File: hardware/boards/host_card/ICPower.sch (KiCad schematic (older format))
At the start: 56 parts, among them J6 SODIMM_260, U1 ECP5UM5G-381caBGA, U3 CYUSB3014, U4 IS43TR16256B-125KBL, U5 128MiB, U6 128MiB, U7 SI5330B, U8 IS43TR16256B-125KBL

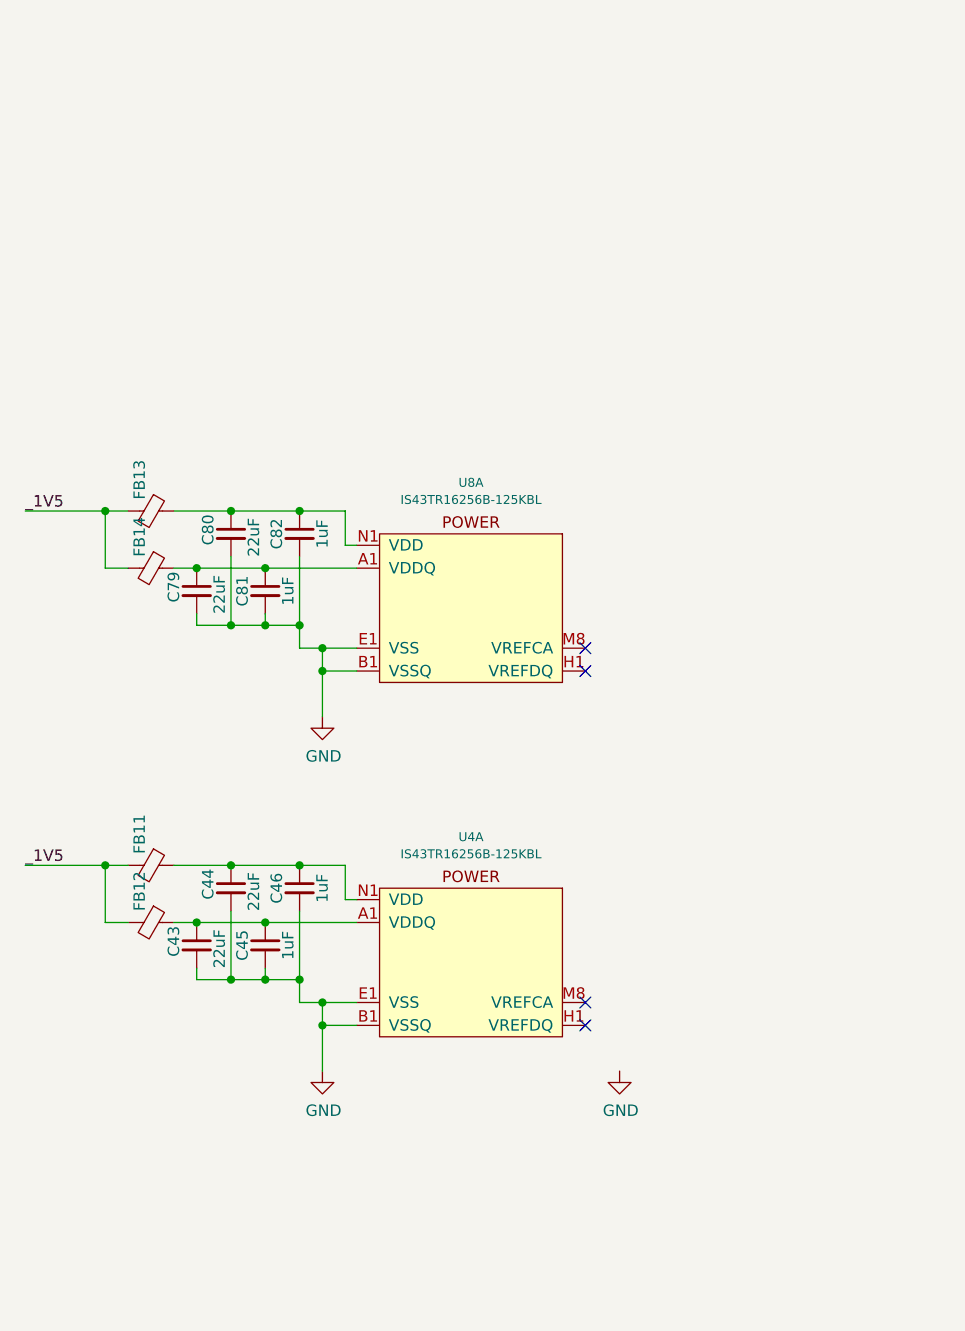
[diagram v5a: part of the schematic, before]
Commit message: Broke out the DDR3 modules and added the 0.75V LDO for the VREFCA and VREFDQ lines for each of the DDR3 modules
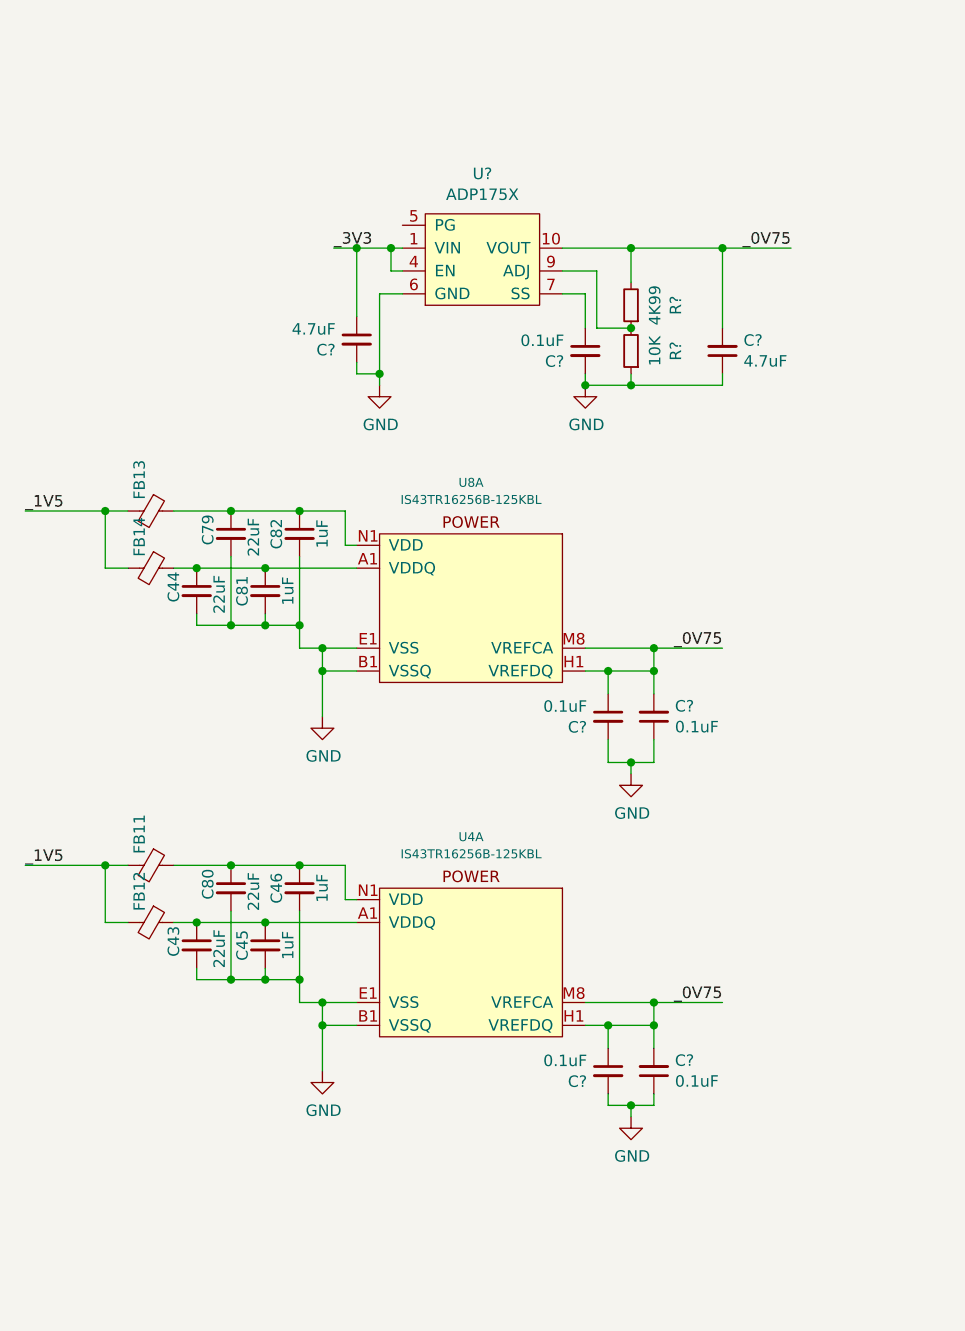
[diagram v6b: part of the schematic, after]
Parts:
- added C? (x5): 0.1uF, Capacitor_SMD:C_0603_1608Metric, symbol Device:C_Small
- added C? (x2): 4.7uF, Capacitor_SMD:C_0603_1608Metric, symbol Device:C_Small
- added R?: 10K, Resistor_SMD:R_0603_1608Metric, symbol Device:R_Small
- added R?: 4K99, Resistor_SMD:R_0603_1608Metric, symbol Device:R_Small
- added U?: ADP175X, Package_DFN_QFN:QFN-16-1EP_4x4mm_P0.65mm_EP2.5x2.5mm, symbol lethalbit:ADP175X
- C43, C44, C79, C80: footprint Capacitor_SMD:C_1206_3216Metric -> Capacitor_SMD:C_0805_2012Metric; MPN C1206C226K9PACTU -> C0805C226K9PAC7800
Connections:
- net 3V3: now also C?.1, U?.1 (VIN), U?.15 (VIN), U?.16 (VIN), U?.2 (VIN), U?.3 (VIN), U?.4 (EN)
- net GND: now also C?.1, C?.1, C?.1, C?.2, C?.2, C?.2, C?.2, R?.1, U?.17 (GND), U?.6 (GND)
- net at C46.1, FB11.1, U4.B2 (VDD)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: now also C80.1; no longer C44.1
- net _0V75: now reaches U4.H1 (VREFDQ)
- net _0V75: now also U4.M8 (VREFCA), U8.H1 (VREFDQ), U8.M8 (VREFCA), C?.1, C?.1, C?.2, C?.2, C?.2, R?.2, U?.10 (VOUT), U?.11 (VOUT), U?.12 (VOUT), U?.13 (VOUT), U?.14 (VOUT)
- net at C81.1, FB14.1, U8.A1 (VDDQ)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: now also C44.1; no longer C79.1
- net at C82.1, FB13.1, U8.B2 (VDD)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: now also C79.1; no longer C80.1
- new net: C?.1, U?.7 (SS)
- new net: R?.1, R?.2, U?.9 (ADJ)
- no-connect marks 10 -> 6

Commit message: Minor cleanup and added some notes
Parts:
- gave numbers to parts that had none: 10
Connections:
- no-connect marks 6 -> 1
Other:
- note added: "TODO: Add the appropriate voltage levels for each bank\n"
- note added: "TODO: Properly add the rest of the bypass caps for the rest of the IO banks."
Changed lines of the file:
@@
 $EndDescr
-$Comp
-L lethalbit:LFE5UM5G-85F-8BG381I U?
-U 1 1 5F21FED7
-P 8500 1700
-AR Path="/5F21FED7" Ref="U?"  Part="1"
-AR Path="/5EF66251/5F21FED7" Ref="U?"  Part="1"
-AR Path="/5EF66188/5F21FED7" Ref="U1"  Part="1"
-F 0 "U1" H 8475 2048 50  0000 C CNN
-F 1 "ECP5UM5G-381caBGA" H 8475 1957 50  0000 C CNN
-F 2 "lethalbit:318caBGA" H 7150 1850 50  0001 C CNN
-F 3 "" H 7150 1850 50  0001 C CNN
-F 4 "Lattice" H 8500 1700 50  0001 C CNN "MFR"
-F 5 "LFE5UM5G-85F-8BG381I" H 8500 1700 50  0001 C CNN "MPN"
-F 6 "220-2112-ND" H 8500 1700 50  0001 C CNN "DIGIKEY_PN"
-	1    8500 1700
-	1    0    0    -1
-$EndComp
 $Comp
 L lethalbit:CYUSB3014 U3
@@
 Wire Wire Line
 	9100 1650 9600 1650
-NoConn ~ 7850 2200
-NoConn ~ 7850 1800
-NoConn ~ 9100 2000
-NoConn ~ 9100 2150
 $Comp
 L Device:C_Small C40
@@
 Text Label 700  9550 0    39   ~ 0
 _3V3
-NoConn ~ 9100 1800
 Wire Wire Line
 	5200 4800 5150 4800
@@
 Wire Wire Line
 	9100 2750 9600 2750
-NoConn ~ 9100 2600
 $Comp
 L lethalbit:SODIMM_260 J6
@@
 	9200 6300 9500 6300
 $Comp
-L lethalbit:ADP175X U?
+L lethalbit:ADP175X U9
 U 1 1 5F9DE092
 P 10300 5150
-F 0 "U?" H 10300 5475 50  0000 C CNN
+F 0 "U9" H 10300 5475 50  0000 C CNN
 F 1 "ADP175X" H 10300 5384 50  0000 C CNN
 F 2 "Package_DFN_QFN:QFN-16-1EP_4x4mm_P0.65mm_EP2.5x2.5mm" H 10300 4750 50  0001 C CNN
@@
 P 10750 5600
 AR Path="/5EDF9F51/5FA82CDE" Ref="C?"  Part="1"
-AR Path="/5EF66188/5FA82CDE" Ref="C?"  Part="1"
-F 0 "C?" H 10658 5554 50  0000 R CNN
+AR Path="/5EF66188/5FA82CDE" Ref="C85"  Part="1"
+F 0 "C85" H 10658 5554 50  0000 R CNN
 F 1 "0.1uF" H 10658 5645 50  0000 R CNN
 F 2 "Capacitor_SMD:C_0603_1608Metric" H 10750 5600 50  0001 C CNN
@@
 	10750 5350 10650 5350
 $Comp
-L power:GND #PWR?
+L power:GND #PWR0149
 U 1 1 5FAB1A8D
 P 10750 5750
-F 0 "#PWR?" H 10750 5500 50  0001 C CNN
+F 0 "#PWR0149" H 10750 5500 50  0001 C CNN
 F 1 "GND" H 10755 5577 50  0000 C CNN
 F 2 "" H 10750 5750 50  0001 C CNN
@@
 P 11350 5600
 AR Path="/5EDF9F51/5FB87077" Ref="C?"  Part="1"
-AR Path="/5EF66188/5FB87077" Ref="C?"  Part="1"
-F 0 "C?" H 11258 5554 50  0000 R CNN
+AR Path="/5EF66188/5FB87077" Ref="C90"  Part="1"
+F 0 "C90" H 11258 5554 50  0000 R CNN
 F 1 "4.7uF" H 11258 5645 50  0000 R CNN
 F 2 "Capacitor_SMD:C_0603_1608Metric" H 11350 5600 50  0001 C CNN
@@
 P 9750 5550
 AR Path="/5EDF9F51/5FB96633" Ref="C?"  Part="1"
-AR Path="/5EF66188/5FB96633" Ref="C?"  Part="1"
-F 0 "C?" H 9658 5504 50  0000 R CNN
+AR Path="/5EF66188/5FB96633" Ref="C84"  Part="1"
+F 0 "C84" H 9658 5504 50  0000 R CNN
 F 1 "4.7uF" H 9658 5595 50  0000 R CNN
 F 2 "Capacitor_SMD:C_0603_1608Metric" H 9750 5550 50  0001 C CNN
@@
 P 10950 5600
 AR Path="/5EDF9F51/5FC1B035" Ref="R?"  Part="1"
-AR Path="/5EF66188/5FC1B035" Ref="R?"  Part="1"
-F 0 "R?" V 10754 5600 50  0000 C CNN
+AR Path="/5EF66188/5FC1B035" Ref="R64"  Part="1"
+F 0 "R64" V 10754 5600 50  0000 C CNN
 F 1 "10K" V 10845 5600 50  0000 C CNN
 F 2 "Resistor_SMD:R_0603_1608Metric" H 10950 5600 50  0001 C CNN
@@
 P 10950 5400
 AR Path="/5EDF9F51/5FC4D903" Ref="R?"  Part="1"
-AR Path="/5EF66188/5FC4D903" Ref="R?"  Part="1"
-F 0 "R?" V 10754 5400 50  0000 C CNN
+AR Path="/5EF66188/5FC4D903" Ref="R63"  Part="1"
+F 0 "R63" V 10754 5400 50  0000 C CNN
 F 1 "4K99" V 10845 5400 50  0000 C CNN
 F 2 "Resistor_SMD:R_0603_1608Metric" H 10950 5400 50  0001 C CNN
@@
 P 10850 7200
 AR Path="/5EDF9F51/5FE759F1" Ref="C?"  Part="1"
-AR Path="/5EF66188/5FE759F1" Ref="C?"  Part="1"
-F 0 "C?" H 10758 7154 50  0000 R CNN
+AR Path="/5EF66188/5FE759F1" Ref="C86"  Part="1"
+F 0 "C86" H 10758 7154 50  0000 R CNN
 F 1 "0.1uF" H 10758 7245 50  0000 R CNN
 F 2 "Capacitor_SMD:C_0603_1608Metric" H 10850 7200 50  0001 C CNN
@@
 P 11050 7200
 AR Path="/5EDF9F51/5FE8FAB1" Ref="C?"  Part="1"
-AR Path="/5EF66188/5FE8FAB1" Ref="C?"  Part="1"
-F 0 "C?" H 10958 7154 50  0000 R CNN
+AR Path="/5EF66188/5FE8FAB1" Ref="C88"  Part="1"
+F 0 "C88" H 10958 7154 50  0000 R CNN
 F 1 "0.1uF" H 10958 7245 50  0000 R CNN
 F 2 "Capacitor_SMD:C_0603_1608Metric" H 11050 7200 50  0001 C CNN
@@
 P 10850 8750
 AR Path="/5EDF9F51/5FEB3A4F" Ref="C?"  Part="1"
-AR Path="/5EF66188/5FEB3A4F" Ref="C?"  Part="1"
-F 0 "C?" H 10758 8704 50  0000 R CNN
+AR Path="/5EF66188/5FEB3A4F" Ref="C87"  Part="1"
+F 0 "C87" H 10758 8704 50  0000 R CNN
 F 1 "0.1uF" H 10758 8795 50  0000 R CNN
 F 2 "Capacitor_SMD:C_0603_1608Metric" H 10850 8750 50  0001 C CNN
@@
 P 11050 8750
 AR Path="/5EDF9F51/5FEB3A57" Ref="C?"  Part="1"
-AR Path="/5EF66188/5FEB3A57" Ref="C?"  Part="1"
-F 0 "C?" H 10958 8704 50  0000 R CNN
+AR Path="/5EF66188/5FEB3A57" Ref="C89"  Part="1"
+F 0 "C89" H 10958 8704 50  0000 R CNN
 F 1 "0.1uF" H 10958 8795 50  0000 R CNN
 F 2 "Capacitor_SMD:C_0603_1608Metric" H 11050 8750 50  0001 C CNN
@@
 $EndComp
 $Comp
-L power:GND #PWR?
+L power:GND #PWR0150
 U 1 1 5FECF713
 P 10950 7450
-F 0 "#PWR?" H 10950 7200 50  0001 C CNN
+F 0 "#PWR0150" H 10950 7200 50  0001 C CNN
 F 1 "GND" H 10955 7277 50  0000 C CNN
 F 2 "" H 10950 7450 50  0001 C CNN
@@
 	10950 7400 10950 7450
 $Comp
-L power:GND #PWR?
+L power:GND #PWR0151
 U 1 1 5FF16D2A
 P 10950 8950
-F 0 "#PWR?" H 10950 8700 50  0001 C CNN
+F 0 "#PWR0151" H 10950 8700 50  0001 C CNN
 F 1 "GND" H 10955 8777 50  0000 C CNN
 F 2 "" H 10950 8950 50  0001 C CNN
@@
 Text Label 11350 8450 2    50   ~ 0
 _0V75
+NoConn ~ 9950 5050
+Text Notes 8650 1000 0    50   ~ 0
+TODO: Properly add the rest of the bypass caps for the rest of the IO banks.
+Text Notes 8650 1100 0    50   ~ 0
+TODO: Add the appropriate voltage levels for each bank\n
+$Comp
+L lethalbit:LFE5UM5G-85F-8BG381I U?
+U 1 1 5F21FED7
+P 8500 1700
+AR Path="/5F21FED7" Ref="U?"  Part="1"
+AR Path="/5EF66251/5F21FED7" Ref="U?"  Part="1"
+AR Path="/5EF66188/5F21FED7" Ref="U1"  Part="1"
+F 0 "U1" H 8475 2048 50  0000 C CNN
+F 1 "ECP5UM5G-381caBGA" H 8475 1957 50  0000 C CNN
+F 2 "lethalbit:318caBGA" H 7150 1850 50  0001 C CNN
+F 3 "" H 7150 1850 50  0001 C CNN
+F 4 "Lattice" H 8500 1700 50  0001 C CNN "MFR"
+F 5 "LFE5UM5G-85F-8BG381I" H 8500 1700 50  0001 C CNN "MPN"
+F 6 "220-2112-ND" H 8500 1700 50  0001 C CNN "DIGIKEY_PN"
+	1    8500 1700
+	1    0    0    -1
+$EndComp
 $EndSCHEMATC

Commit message: Commited unholy DDR3 routing crimes
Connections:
- net at C43.1, C45.1, FB12.1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: now also C46.1, C80.1, FB11.1, U4.B2 (VDD), U4.D9 (VDD), U4.G7 (VDD), U4.K2 (VDD), U4.K8 (VDD), U4.N1 (VDD), U4.N9 (VDD), U4.R1 (VDD), U4.R9 (VDD)
- net at C44.1, C81.1, FB14.1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: now also C79.1, C82.1, FB13.1, U8.B2 (VDD), U8.D9 (VDD), U8.G7 (VDD), U8.K2 (VDD), U8.K8 (VDD), U8.N1 (VDD), U8.N9 (VDD), U8.R1 (VDD), U8.R9 (VDD)
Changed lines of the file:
@@
 Connection ~ 9600 6900
 Wire Wire Line
-	8950 6300 9200 6300
-Wire Wire Line
-	8950 6550 9050 6550
-Wire Wire Line
-	8950 7850 9200 7850
+	8950 7850 9050 7850
 $Comp
 L Device:C_Small C?
@@
 	1    0    0    -1
 $EndComp
+Wire Wire Line
+	8950 6550 9050 6550
+Wire Wire Line
+	8950 6300 9050 6300
+Wire Wire Line
+	9050 6550 9050 6300
+Connection ~ 9050 6300
+Wire Wire Line
+	9050 6300 9200 6300
+Wire Wire Line
+	9050 8100 9050 7850
+Connection ~ 9050 7850
+Wire Wire Line
+	9050 7850 9200 7850
 $EndSCHEMATC
